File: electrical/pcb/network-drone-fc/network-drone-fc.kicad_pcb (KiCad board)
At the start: 4 copper layers, 36 x 36 mm, 4 parts

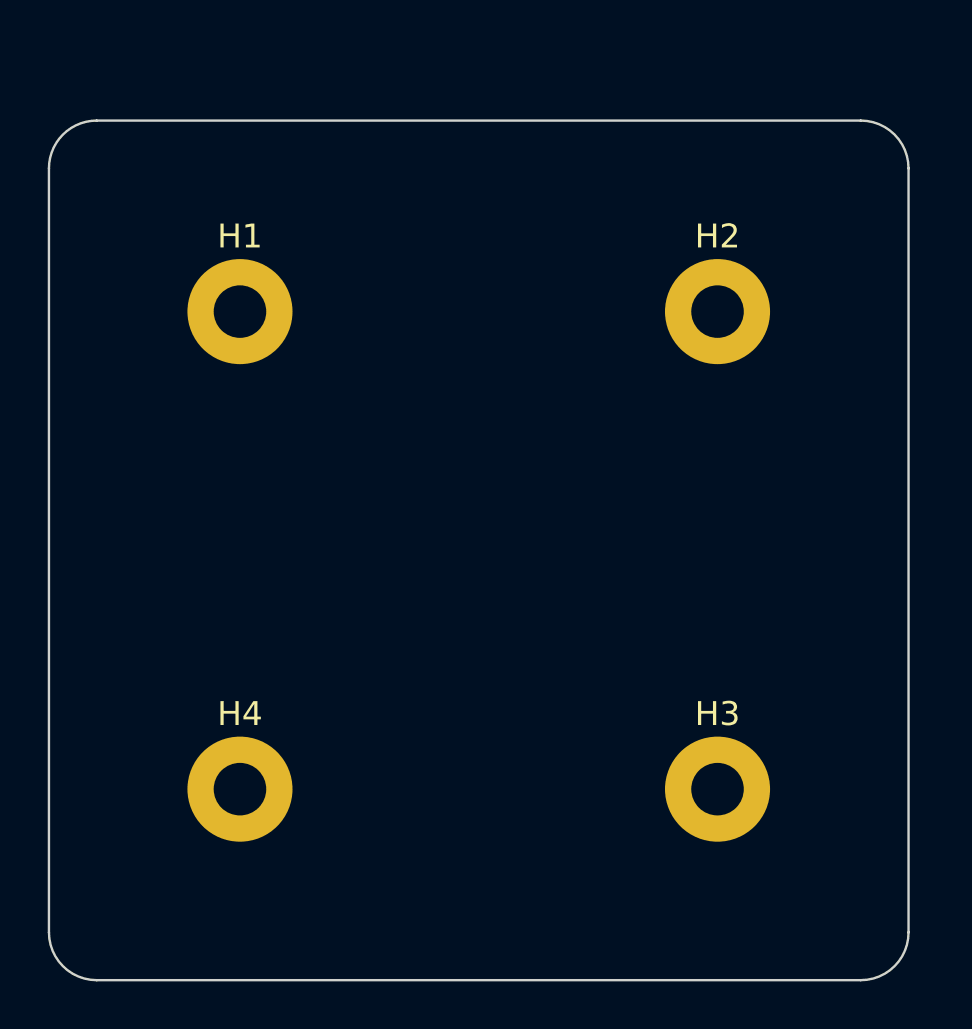
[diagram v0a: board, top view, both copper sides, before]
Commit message: PCB: place every part on the 36x36 board, nets from the schematic, rules set
All parts on the top side per the floorplan: IMU centre, ESP32 right with its
decoupling column and crystal, GPS top with its U.FL at the corner, buck above
the ESC connector, ports on the edges, test pads on the bottom. Plain NPTH M2
holes. DRC: no clearance, edge or courtyard errors; routing still to do.
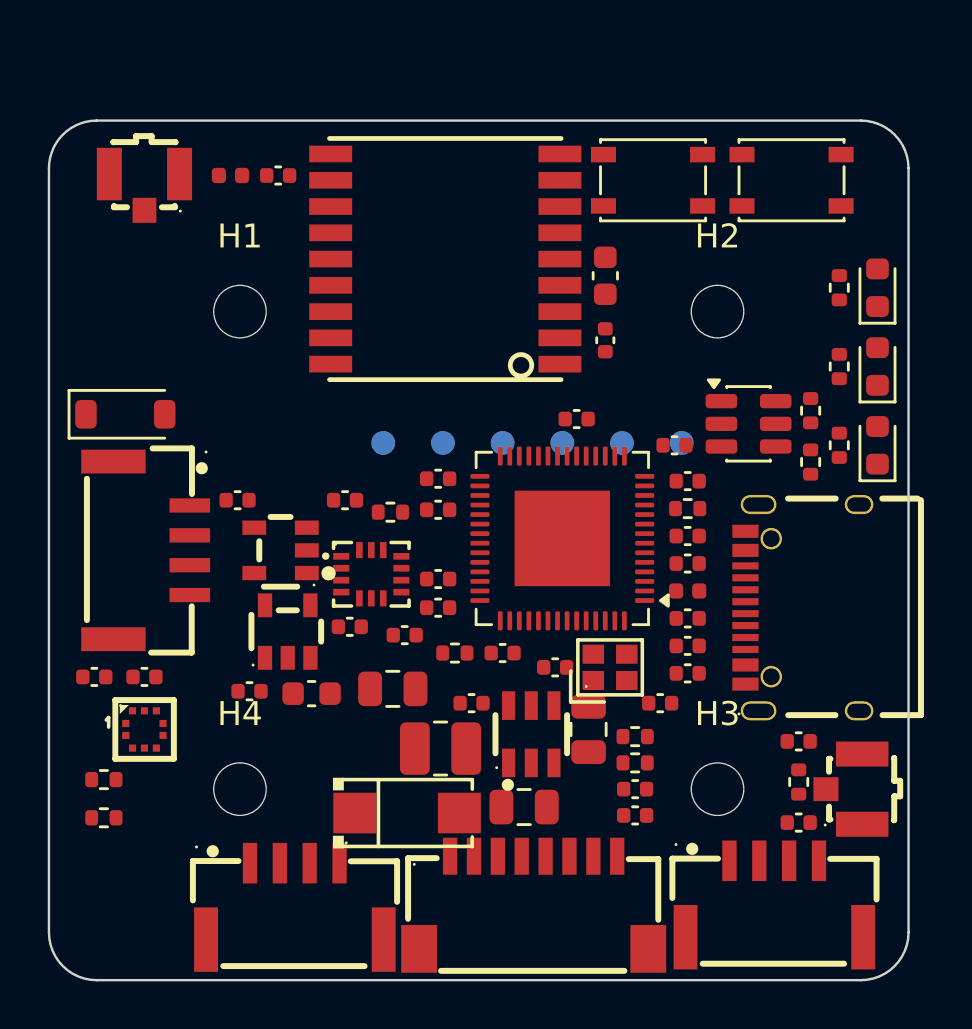
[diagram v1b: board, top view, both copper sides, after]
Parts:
- added C1: 0.1uF, C_0402_1005Metric, F.Cu at (108.8, 102.8)
- added C10: 1uF, C_0402_1005Metric, F.Cu at (98.3, 98.3)
- added C11: 1uF, C_0402_1005Metric, F.Cu at (108.8, 97.1)
- added C12: 15pF, C_0402_1005Metric, F.Cu at (103.2, 104.9)
- added C13: 15pF, C_0402_1005Metric, F.Cu at (107.6, 106.4)
- added C14: DNP, C_0402_1005Metric, F.Cu at (113.4, 108.0)
- added C15: DNP, C_0402_1005Metric, F.Cu at (113.4, 111.4)
- added C16: 10uF 25V, C_0805_2012Metric, F.Cu at (104.6, 107.5)
- added C17: 100nF, C_0402_1005Metric, F.Cu at (99.7, 106.4)
- added C18: 22uF 10V, C_0805_2012Metric, F.Cu at (101.9, 110.8)
- added C19: 22uF 10V, C_0805_2012Metric, F.Cu at (96.4, 105.8)
- added C2: 0.1uF, C_0402_1005Metric, F.Cu at (108.8, 100.5)
- added C20: 1uF, C_0402_1005Metric, F.Cu at (90.4, 105.9)
- added C21: 1uF, C_0402_1005Metric, F.Cu at (94.6, 103.2)
- added C22: 1uF, C_0402_1005Metric, F.Cu at (89.9, 97.9)
- added C23: 1uF, C_0402_1005Metric, F.Cu at (94.4, 97.9)
- added C24: 100nF, C_0402_1005Metric, F.Cu at (106.5, 110.0)
- added C25: 0.1uF, C_0402_1005Metric, F.Cu at (98.3, 101.2)
- added C26: 2.2uF, C_0402_1005Metric, F.Cu at (98.3, 102.4)
- added C27: 10nF, C_0402_1005Metric, F.Cu at (96.9, 103.5)
- added C28: 100nF, C_0402_1005Metric, F.Cu at (86.0, 105.3)
- added C29: 100nF, C_0402_1005Metric, F.Cu at (83.9, 105.3)
- added C3: 1uF, C_0402_1005Metric, F.Cu at (108.8, 99.4)
- added C30: 10uF, C_0603_1608Metric, F.Cu at (105.3, 88.5)
- added C31: 100nF, C_0402_1005Metric, F.Cu at (105.3, 91.2)
- added C32: 10nF, C_0402_1005Metric, F.Cu at (91.6, 84.3)
- added C33: 100nF, C_0402_1005Metric, F.Cu at (106.5, 111.1)
- added C34: 100nF, C_0402_1005Metric, F.Cu at (108.2, 95.6)
- added C4: 10uF 6.3V, C_0603_1608Metric, F.Cu at (93.0, 106.0)
- added C5: 1uF, C_0402_1005Metric, F.Cu at (108.8, 104.0)
- added C6: 10nF, C_0402_1005Metric, F.Cu at (108.8, 105.2)
- added C7: 0.1uF, C_0402_1005Metric, F.Cu at (104.1, 94.5)
- added C8: 0.1uF, C_0402_1005Metric, F.Cu at (101.0, 104.3)
- added C9: 0.1uF, C_0402_1005Metric, F.Cu at (98.3, 97.0)
- added D1: B5819W, D_SOD-123, F.Cu at (85.2, 94.3)
- added D2: RED, LED_0603_1608Metric, F.Cu at (116.7, 89.0)
- added D3: GREEN, LED_0603_1608Metric, F.Cu at (116.7, 92.3)
- added D4: YELLOW, LED_0603_1608Metric, F.Cu at (116.7, 95.6)
- added D5: SMAJ18A, SMA_L4.4-W2.6-LS5.0-RD, F.Cu at (97.0, 111.0)
- added J1: U.FL-R-SMT-1, RF-SMD_FRF05002-JSS103M, F.Cu at (115.3, 110.0)
- added J2: TYPE-C 16PIN 2MD, USB-C-SMD_TYPE-C-16PIN-2MD-073, F.Cu at (113.5, 102.4)
- added J3: U.FL GPS, RF-SMD_FRF05002-JSS103M, F.Cu at (86.0, 85.0)
- added J4: ESC, CONN-TH_SM08B-SRSS-TB-LF-SN, F.Cu at (102.3, 114.8)
- added J5: I2C port, CONN-SMD_4P-P1.25_SM04B-GHS-TB-LF-SN, F.Cu at (86.3, 100.0)
- added J6: UART port, CONN-SMD_4P-P1.25_SM04B-GHS-TB-LF-SN, F.Cu at (92.3, 114.7)
- added J7: Charging board, CONN-SMD_4P-P1.25_SM04B-GHS-TB-LF-SN, F.Cu at (112.4, 114.6)
- added L1: 2.0nH, L_0402_1005Metric, F.Cu at (108.8, 101.7)
- added L2: 4.7uH, L_1008_2520Metric, F.Cu at (98.4, 108.3)
- added L3: 27nH DNP, L_0402_1005Metric, F.Cu at (89.6, 84.3)
- added R1: 10k, R_0402_1005Metric, F.Cu at (108.8, 98.2)
- added R10: 10k, R_0402_1005Metric, F.Cu at (106.5, 108.9)
- added R11: 10k, R_0402_1005Metric, F.Cu at (96.3, 98.4)
- added R12: 4.7k, R_0402_1005Metric, F.Cu at (84.3, 109.6)
- added R13: 4.7k, R_0402_1005Metric, F.Cu at (84.3, 111.2)
- added R2: 0, R_0402_1005Metric, F.Cu at (99.0, 104.3)
- added R3: 0, R_0402_1005Metric, F.Cu at (113.4, 109.7)
- added R4: 5.1k, R_0402_1005Metric, F.Cu at (113.9, 94.2)
- added R5: 5.1k, R_0402_1005Metric, F.Cu at (113.9, 96.3)
- added R6: 1k, R_0402_1005Metric, F.Cu at (115.1, 89.0)
- added R7: 470, R_0402_1005Metric, F.Cu at (115.1, 92.3)
- added R8: 1k, R_0402_1005Metric, F.Cu at (115.1, 95.6)
- added R9: 100k, R_0402_1005Metric, F.Cu at (106.5, 107.8)
- added SW1: RESET, SW_SPST_PTS810, F.Cu at (113.1, 84.5)
- added SW2: BOOT, SW_SPST_PTS810, F.Cu at (107.3, 84.5)
- added TP1: TestPoint, TestPoint_Pad_D1.0mm, B.Cu at (96.0, 95.5)
- added TP2: TestPoint, TestPoint_Pad_D1.0mm, B.Cu at (98.5, 95.5)
- added TP3: TestPoint, TestPoint_Pad_D1.0mm, B.Cu at (101.0, 95.5)
- added TP4: TestPoint, TestPoint_Pad_D1.0mm, B.Cu at (103.5, 95.5)
- added TP5: TestPoint, TestPoint_Pad_D1.0mm, B.Cu at (106.0, 95.5)
- added TP6: TestPoint, TestPoint_Pad_D1.0mm, B.Cu at (108.5, 95.5)
- added U1: ESP32-S3FN8, QFN-56-1EP_7x7mm_P0.4mm_EP4x4mm, F.Cu at (103.5, 99.5)
- added U2: USBLC6-2SC6, SOT-23-6, F.Cu at (111.3, 94.7)
- added U3: AP63205WU-7, TSOT-23-6_L2.9-W1.6-P0.95-LS2.8-BL, F.Cu at (102.2, 107.7)
- added U4: TLV75733PDBVR, SOT-23-5_L2.9-W1.6-P0.95-LS2.8-BL, F.Cu at (92.0, 103.4)
- added U5: TPS7A2033PDBVR, SOT-23-5_L2.9-W1.6-P0.95-LS2.8-BR, F.Cu at (91.7, 100.0)
- added U6: ICM-42688-P, LGA-14_L3.0-W2.5-P0.50-TL, F.Cu at (95.5, 101.0)
- added U7: BMP581, LGA-10_L2.0-W2.0-P0.50-TL_BMP581, F.Cu at (86.0, 107.5)
- added U8: MAX-M10S, SMD-18_L10.1-W9.7-P1.10-TL_SKG09F, F.Cu at (98.6, 87.8)
- added X1: Q22FA12800101, CRYSTAL-SMD_4P-L2.0-W1.6-BL, F.Cu at (105.5, 104.9)
- H1, H2, H3, H4: value MountingHole_2.2mm_M2_Pad -> M2; footprint MountingHole:MountingHole_2.2mm_M2_Pad -> MountingHole:MountingHole_2.2mm_M2
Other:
- board text added: "Pranav Shivashankar"
- board text added: "TAR Team 1 network drone FC rev A"

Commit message: Pads instead of buttons, twelve more test points, 3 mm hole keep-out
RESET/BOOT become JP1/JP2 solder-jumper pad pairs on the bottom. TP7-TP18 bring
the IMU SPI bus, I2C, GPS UART, ESC telemetry and the spare UART to bottom-side
pads. The spare UART connector J6 is dropped: with 3 mm clear around each hole
for grommets, the board has one connector slot per edge. Charging port moves to
the top right. DRC: no copper errors.
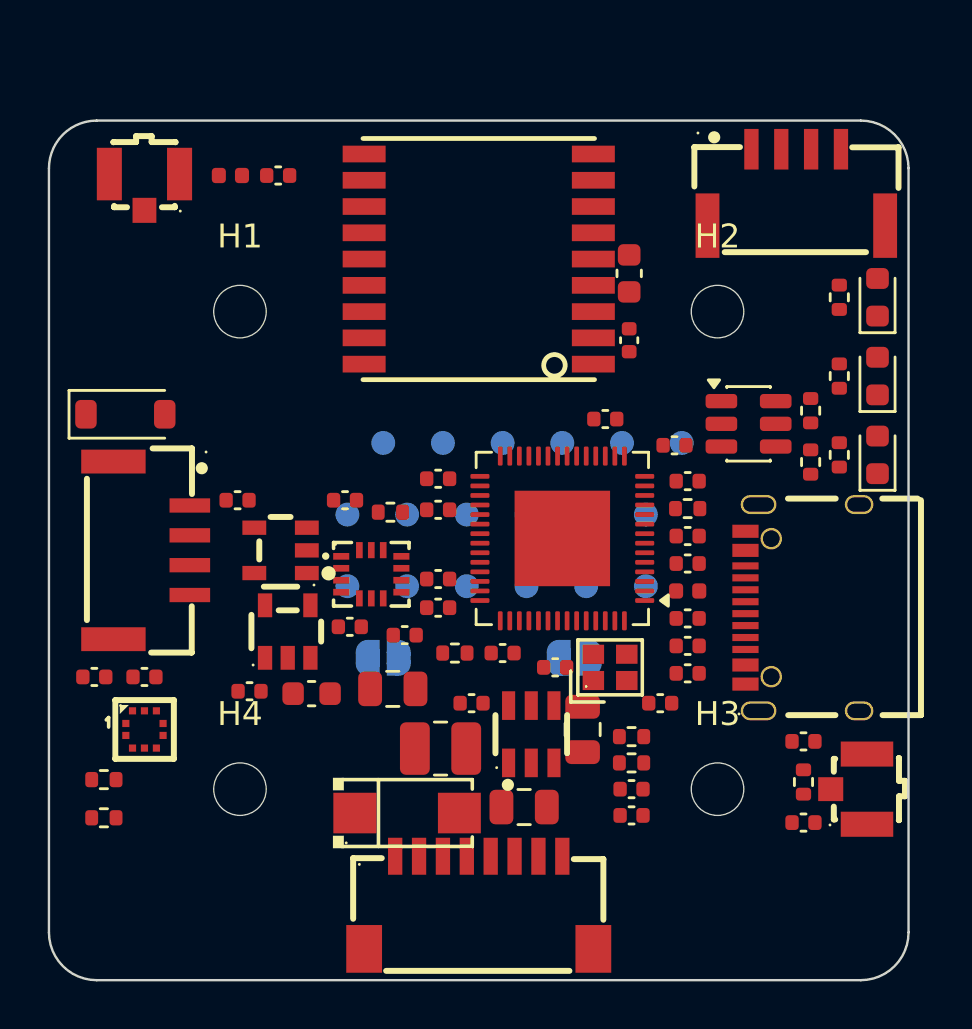
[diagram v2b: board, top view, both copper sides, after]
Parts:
- removed J6: UART port, CONN-SMD_4P-P1.25_SM04B-GHS-TB-LF-SN
- removed SW1: RESET, SW_SPST_PTS810
- removed SW2: BOOT, SW_SPST_PTS810
- added JP1: RESET, Jumper:SolderJumper-2_P1.3mm_Open_RoundedPad1.0x1.5mm, B.Cu at (96.0, 104.5)
- added JP2: BOOT, Jumper:SolderJumper-2_P1.3mm_Open_RoundedPad1.0x1.5mm, B.Cu at (104.0, 104.5)
- added TP10: TestPoint, TestPoint:TestPoint_Pad_D1.0mm, B.Cu at (102.0, 98.5)
- added TP11: TestPoint, TestPoint:TestPoint_Pad_D1.0mm, B.Cu at (104.5, 98.5)
- added TP12: TestPoint, TestPoint:TestPoint_Pad_D1.0mm, B.Cu at (107.0, 98.5)
- added TP13: TestPoint, TestPoint:TestPoint_Pad_D1.0mm, B.Cu at (94.5, 101.5)
- added TP14: TestPoint, TestPoint:TestPoint_Pad_D1.0mm, B.Cu at (97.0, 101.5)
- added TP15: TestPoint, TestPoint:TestPoint_Pad_D1.0mm, B.Cu at (99.5, 101.5)
- added TP16: TestPoint, TestPoint:TestPoint_Pad_D1.0mm, B.Cu at (102.0, 101.5)
- added TP17: TestPoint, TestPoint:TestPoint_Pad_D1.0mm, B.Cu at (104.5, 101.5)
- added TP18: TestPoint, TestPoint:TestPoint_Pad_D1.0mm, B.Cu at (107.0, 101.5)
- added TP7: TestPoint, TestPoint:TestPoint_Pad_D1.0mm, B.Cu at (94.5, 98.5)
- added TP8: TestPoint, TestPoint:TestPoint_Pad_D1.0mm, B.Cu at (97.0, 98.5)
- added TP9: TestPoint, TestPoint:TestPoint_Pad_D1.0mm, B.Cu at (99.5, 98.5)
- moved J7 29.8 mm to (113.3, 84.8), turned to 180 degrees
- moved J4 2.30 mm to (100.0, 114.8)
- moved U8 1.40 mm to (100.0, 87.8)
- moved C7 1.20 mm to (105.3, 94.5)
- moved C30 1.00 mm to (106.3, 88.4)
- moved C31 1.00 mm to (106.3, 91.2)
- moved D2 0.40 mm to (116.7, 89.4)
- moved D3 0.40 mm to (116.7, 92.7)
- moved D4 0.40 mm to (116.7, 96.0)
- moved R6 0.40 mm to (115.1, 89.4)
- moved R7 0.40 mm to (115.1, 92.7)
- moved R8 0.40 mm to (115.1, 96.0)
- moved C16 0.25 mm to (104.3, 107.5)
- moved J1 0.20 mm to (115.5, 110.0)
- moved C14 0.20 mm to (113.6, 108.0)
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
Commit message: PCB: GND planes on In1 and bottom; autoroute the signal and 3.3 V nets with Freerouting
Freerouting 2.4.1 ran headless on a DSN with the critical nets removed, so the
antenna paths, crystal, USB pair, buck loop (VBAT, SW, BST, +5V) and the VDD3P3
filter node are untouched for hand routing. 149 of 160 nets routed; MOTOR1-4,
ESC_CUR, SPI_MOSI, I2C_SDA/SCL, one +3V3 and one +3V3_SENS link, and the BOOT
pad still open. Two RF-class clearance nits (0.15/0.18 mm) sit next to the
antenna pads and go away when those nets are routed by hand.
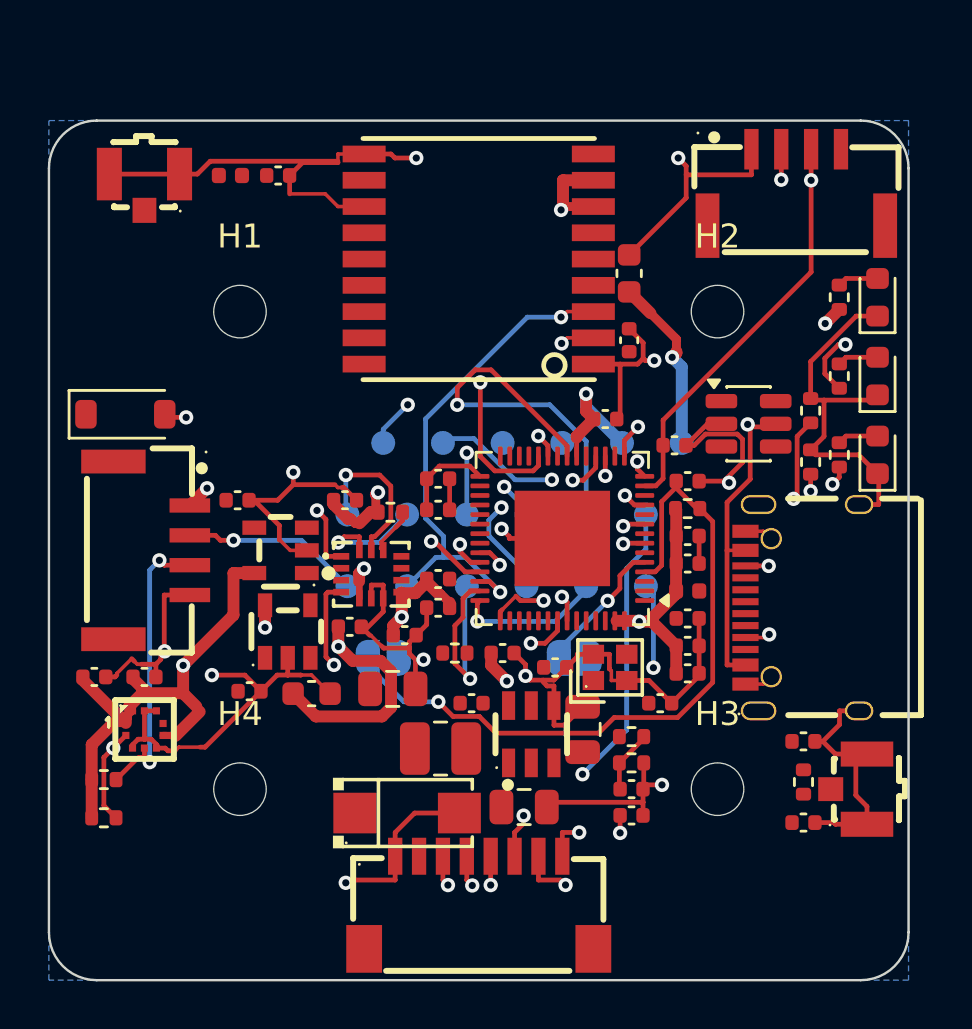
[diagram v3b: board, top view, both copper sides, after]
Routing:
- net GND: track 0.00 -> 149.5 mm, vias 0 -> 12
- net +3V3: track 0.00 -> 93.8 mm, vias 0 -> 7
- net +3V3_SENS: track 0.00 -> 81.9 mm, vias 0 -> 6
- net I2C_SDA: track 0.00 -> 57.1 mm, vias 0 -> 4
- net VBUS: track 0.00 -> 42.7 mm, vias 0 -> 2
- net ICM_INTR: track 0.00 -> 34.2 mm, vias 0 -> 2
- net I2C_SCL: track 0.00 -> 33.7 mm, vias 0 -> 3
- net ESC_CUR: track 0.00 -> 30.5 mm, vias 0 -> 3
- net Net-(JP1-B): track 0.00 -> 30.3 mm, vias 0 -> 1
- net ESC_TELEM: track 0.00 -> 28.1 mm, vias 0 -> 3
- net MOTOR1: track 0.00 -> 25.9 mm, vias 0 -> 2
- net GPS_RX: track 0.00 -> 25.8 mm, vias 0 -> 2
- net DOCK_DET: track 0.00 -> 23.7 mm, vias 0 -> 2
- net Net-(U1-U0TXD): track 0.00 -> 23.3 mm, vias 0 -> 2
- net MOTOR3: track 0.00 -> 23.1 mm, vias 0 -> 2
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- added copper zone on B.Cu, net GND
- added copper zone on In1.Cu, net GND

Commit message: PCB: remove the autoroute; keep placement and GND planes for hand routing
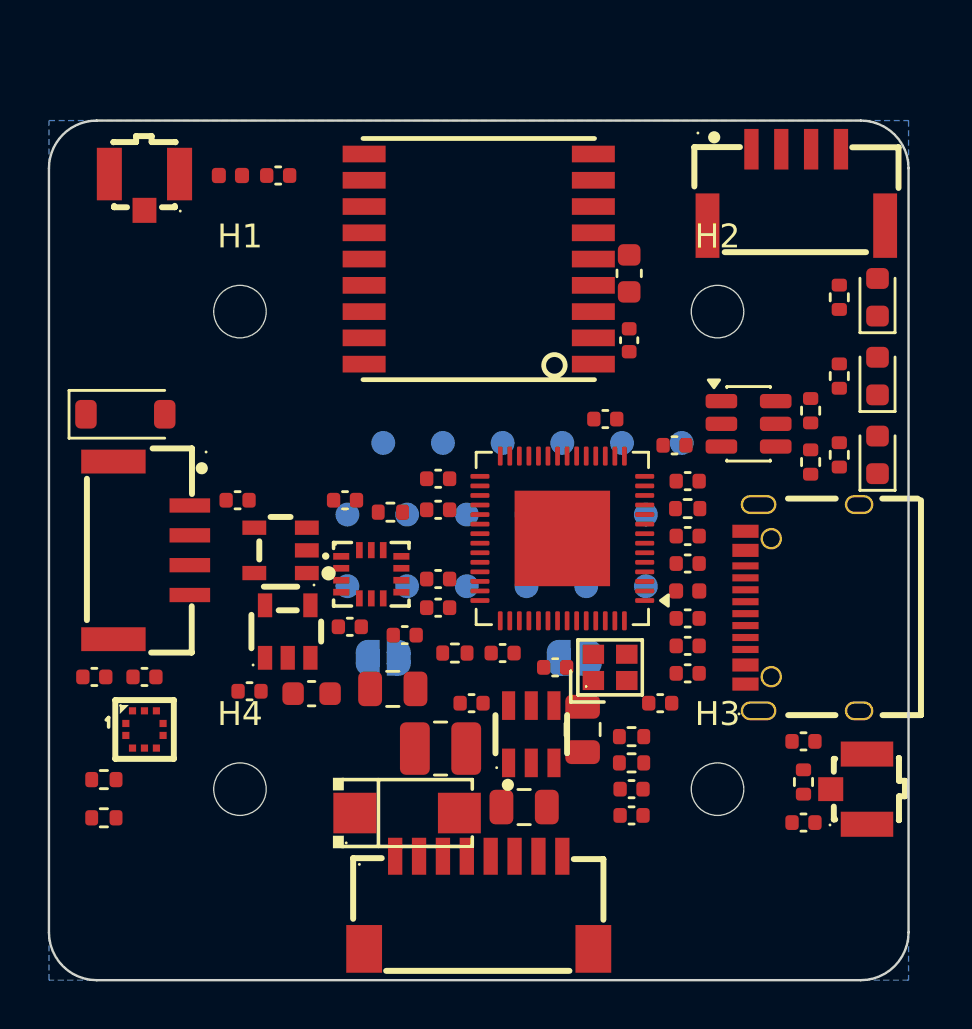
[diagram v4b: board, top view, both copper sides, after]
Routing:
- net GND: track 149.5 -> 0.00 mm, vias 12 -> 0
- net +3V3: track 93.8 -> 0.00 mm, vias 7 -> 0
- net +3V3_SENS: track 81.9 -> 0.00 mm, vias 6 -> 0
- net I2C_SDA: track 57.1 -> 0.00 mm, vias 4 -> 0
- net VBUS: track 42.7 -> 0.00 mm, vias 2 -> 0
- net ICM_INTR: track 34.2 -> 0.00 mm, vias 2 -> 0
- net I2C_SCL: track 33.7 -> 0.00 mm, vias 3 -> 0
- net ESC_CUR: track 30.5 -> 0.00 mm, vias 3 -> 0
- net Net-(JP1-B): track 30.3 -> 0.00 mm, vias 1 -> 0
- net ESC_TELEM: track 28.1 -> 0.00 mm, vias 3 -> 0
- net MOTOR1: track 25.9 -> 0.00 mm, vias 2 -> 0
- net GPS_RX: track 25.8 -> 0.00 mm, vias 2 -> 0
- net DOCK_DET: track 23.7 -> 0.00 mm, vias 2 -> 0
- net Net-(U1-U0TXD): track 23.3 -> 0.00 mm, vias 2 -> 0
- net MOTOR3: track 23.1 -> 0.00 mm, vias 2 -> 0
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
